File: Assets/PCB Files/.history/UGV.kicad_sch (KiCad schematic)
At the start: 68 parts, among them J10 B2B-XH-A, J11 B2B-XH-A, J12 B2B-XH-A, J13 USB3_A, J14 XT30PW-M, J15 Screw_Terminal_01x12, J16 Screw_Terminal_01x12, J17 Screw_Terminal_01x12, J18 Screw_Terminal_01x12, J19 XT30PW-M, J2 Conn_01x24_Socket, J20 XT30PW-M, J21 XT30PW-M, J22 Conn_01x01_Socket, J23 Conn_01x01_Socket, J24 XT30PW-M, J25 B2B-XH-A, J26 B2B-XH-A, J27 B2B-XH-A, J28 B2B-XH-A, J29 B2B-XH-A, J3 Conn_01x24_Socket, J31 B2B-XH-A, J4 Conn_01x02_Pin, J5 B2B-XH-A, J6 B2B-XH-A, J7 B2B-XH-A, J8 B2B-XH-A, J9 B2B-XH-A, Q1 IRLZ44N, U2 LMR33630ADDA, U3 SN74LVC8T245, U4 Teensy4.1

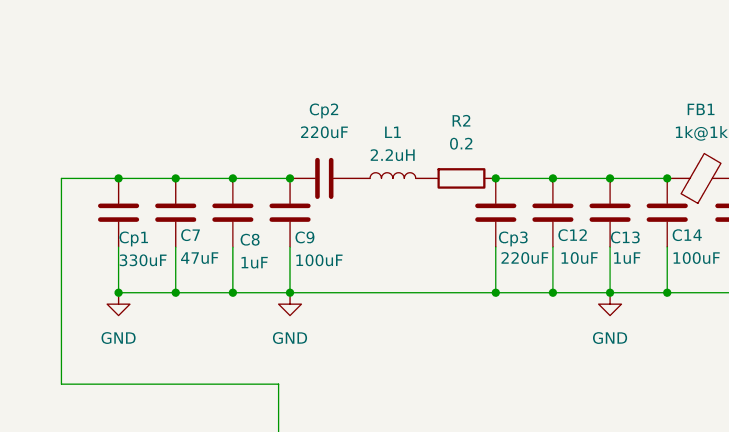
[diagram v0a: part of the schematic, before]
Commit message: Changed Capacitor in LC Filtering
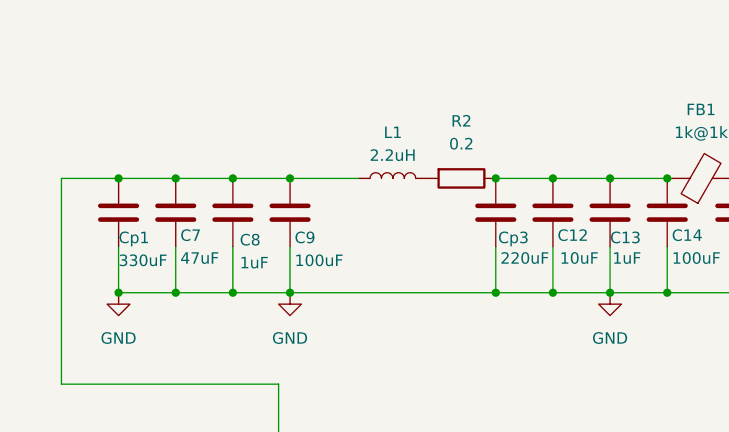
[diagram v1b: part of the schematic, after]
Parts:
- removed Cp2: 220uF, symbol Device:C
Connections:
- net at L1.1: now also C7.1, C8.1, C9.1, Cp1.1, J20.P
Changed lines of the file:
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@@
 	)
 	(junction
-		(at 43.18 27.94)
-		(diameter 0)
-		(color 0 0 0 0)
-	)
-	(junction
 		(at 91.44 120.65)
 		(diameter 0)
@@
 	)
 	(junction
+		(at 43.18 27.94)
+		(diameter 0)
+		(color 0 0 0 0)
+	)
+	(junction
 		(at 229.87 104.14)
 		(diameter 0)
@@
 	(wire
 		(pts
+			(xy 43.18 27.94) (xy 50.8 27.94)
+		)
+		(stroke
+			(width 0)
+			(type default)
+		)
+	)
+	(wire
+		(pts
 			(xy 92.71 40.64) (xy 99.06 40.64)
 		)
@@
 					(unit 1)
 				)
-			)
-		)
-	)
-	(symbol
-		(lib_id "Device:C")
-		(at 46.99 27.94 90)
-		(unit 1)
-		(body_style 1)
-		(exclude_from_sim no)
-		(in_bom yes)
-		(on_board yes)
-		(in_pos_files yes)
-		(dnp no)
-		(fields_autoplaced yes)
-		(property "Reference" "Cp2"
-			(at 46.99 20.32 90)
-			(show_name no)
-			(do_not_autoplace no)
-			(effects
-				(font
-					(size 1.27 1.27)
-				)
-			)
-		)
-		(property "Value" "220uF"
-			(at 46.99 22.86 90)
-			(show_name no)
-			(do_not_autoplace no)
-			(effects
-				(font
-					(size 1.27 1.27)
-				)
-			)
-		)
-		(property "Footprint" ""
-			(at 50.8 26.9748 0)
-			(hide yes)
-			(show_name no)
-			(do_not_autoplace no)
-			(effects
-				(font
-					(size 1.27 1.27)
-				)
-			)
-		)
-		(property "Datasheet" ""
-			(at 46.99 27.94 0)
-			(hide yes)
-			(show_name no)
-			(do_not_autoplace no)
-			(effects
-				(font
-					(size 1.27 1.27)
-				)
-			)
-		)
-		(property "Description" "Unpolarized capacitor"
-			(at 46.99 27.94 0)
-			(hide yes)
-			(show_name no)
-			(do_not_autoplace no)
-			(effects
-				(font
-					(size 1.27 1.27)
-				)
-			)
-		)
-		(pin "2"
-		)
-		(pin "1"
-		)
-		(instances
-			(project "UGV"
-				(path "/07a8edf5-8ac1-4cc3-b758-10bf557c0053"
-					(reference "Cp2")
-					(unit 1)
-				)

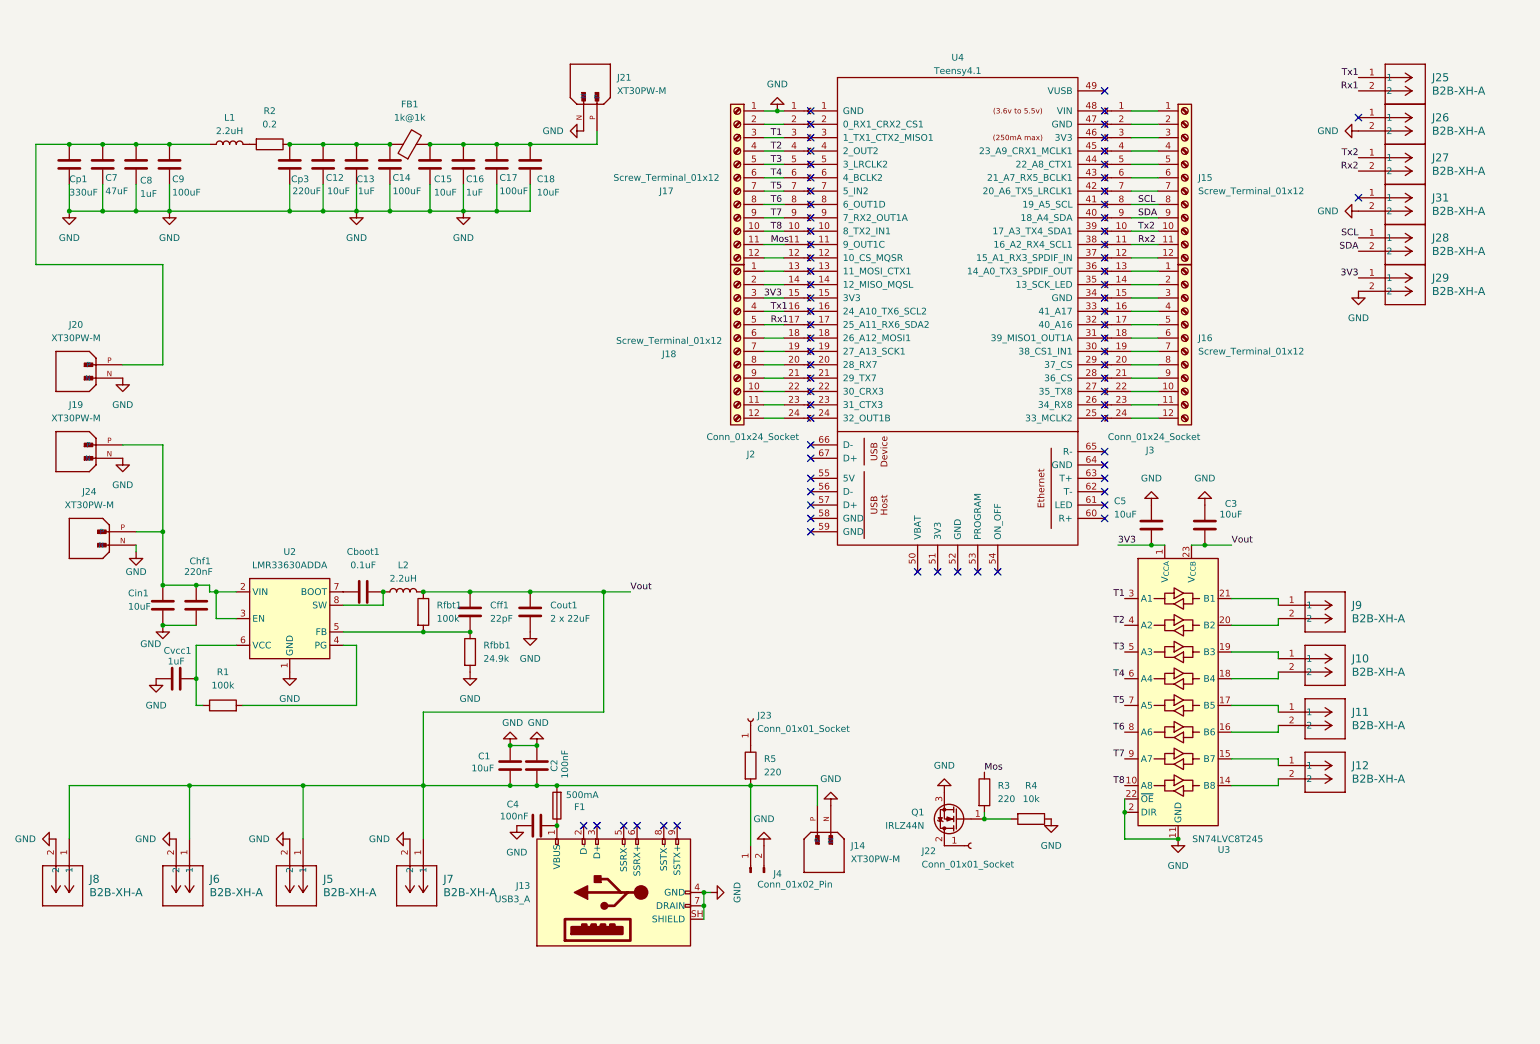
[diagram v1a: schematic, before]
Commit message: Added Custom Model and Updated PCB
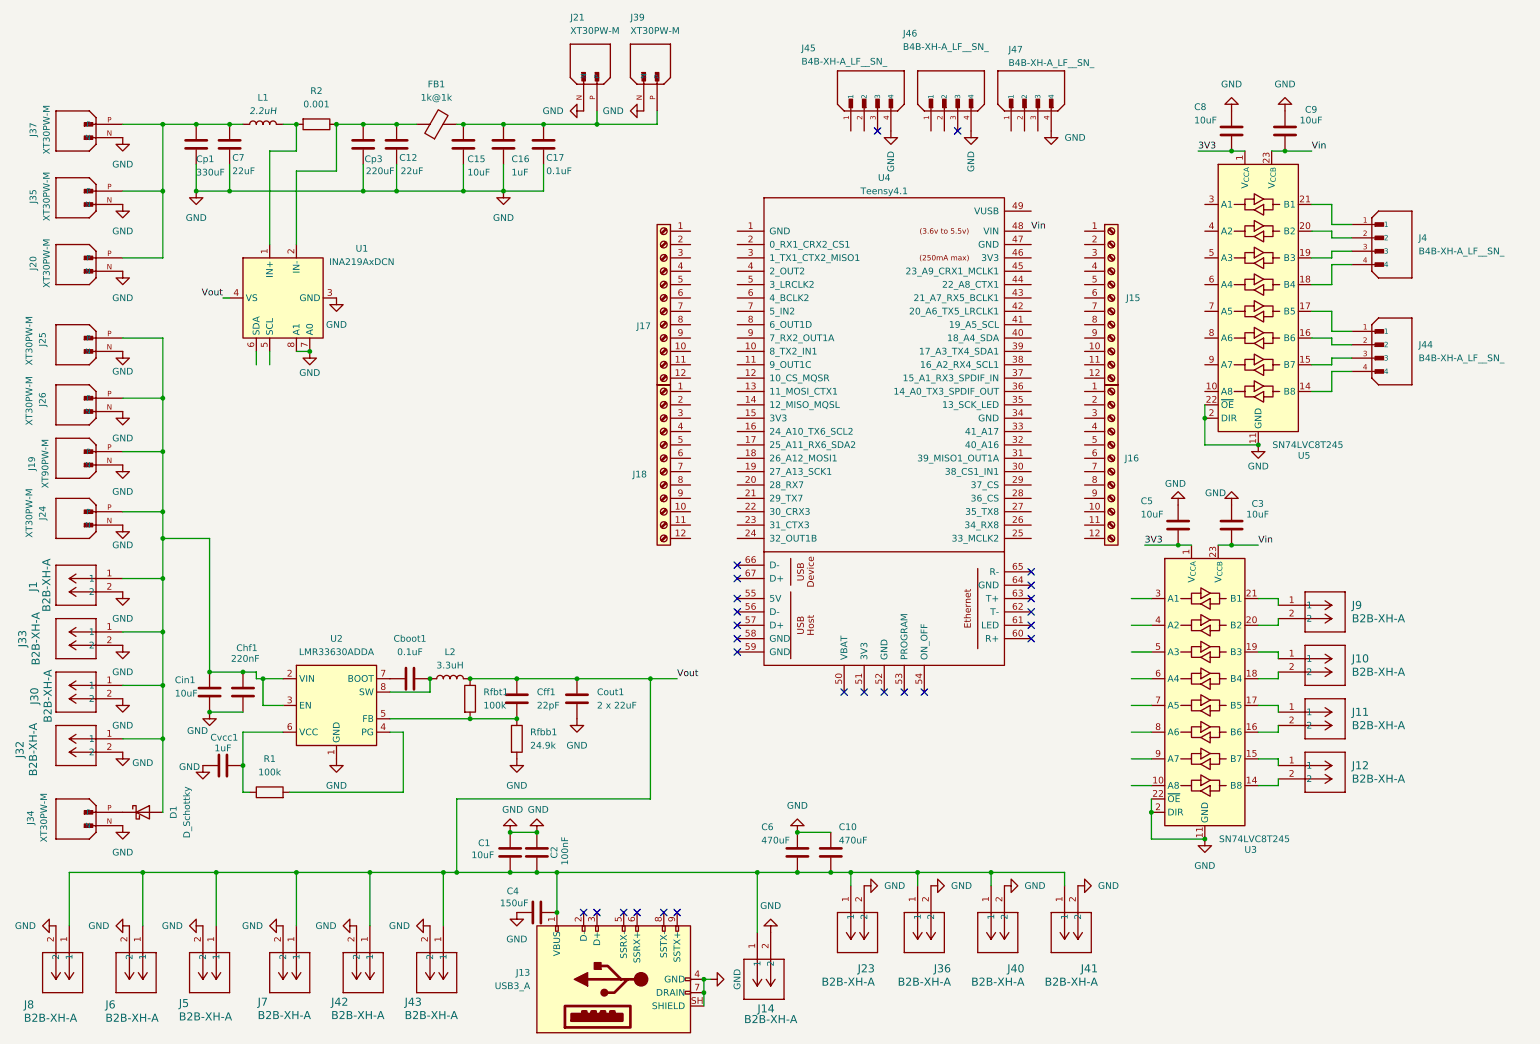
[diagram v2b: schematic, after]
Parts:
- removed C13: 1uF, symbol Device:C
- removed C14: 100uF, symbol Device:C
- removed C18: 10uF, symbol Device:C
- removed F1: 500mA, symbol Device:Fuse
- removed J14: XT30PW-M, Connector_AMASS:AMASS_XT30PW-M_1x02_P2.50mm_Horizontal, symbol XT30PW-M:XT30PW-M
- removed J2, J3: Conn_01x24_Socket, symbol Connector:Conn_01x24_Socket
- removed J22, J23: Conn_01x01_Socket, symbol Connector:Conn_01x01_Socket
- removed J25, J26, J27, J28, J29, J31: B2B-XH-A, Connector_JST:JST_XH_B2B-XH-A_1x02_P2.50mm_Vertical, symbol 2026-03-24_19-43-02:B2B-XH-A
- removed J4: Conn_01x02_Pin, symbol Connector:Conn_01x02_Pin
- removed Q1: IRLZ44N, Package_TO_SOT_THT:TO-220-3_Vertical, symbol Transistor_FET:IRLZ44N
- removed R3, R5: 220, symbol Device:R
- removed R4: 10k, symbol Device:R
- added C10, C6: 470uF, Capacitor_THT:CP_Radial_D8.0mm_P3.50mm, symbol Device:C
- added D1: D_Schottky, Diode_SMD:D_SMC_Handsoldering, symbol Device:D_Schottky
- added J1, J14, J23, J30, J32, J33, J36, J40, J41, J42, J43: B2B-XH-A, Connector_JST:JST_XH_B2B-XH-A_1x02_P2.50mm_Vertical, symbol 2026-03-24_19-43-02:B2B-XH-A
- added J25, J26, J34, J35, J37, J39: XT30PW-M, XT30PW-M (1):AMASS_XT30PW-M, symbol XT30PW-M:XT30PW-M
- added J4, J44, J45, J46, J47: B4B-XH-A_LF__SN_, B4B-XH-A_LF__SN_:JST_B4B-XH-A_LF__SN_, symbol B4B-XH-A_LF__SN_:B4B-XH-A_LF__SN_
- added U1: INA219AxDCN, Package_TO_SOT_SMD:SOT-23-8, symbol Sensor_Energy:INA219AxDCN
- added U5: SN74LVC8T245, SN74LVC8T245DWR:SOIC127P1030X265-24N, symbol Logic_LevelTranslator:SN74LVC8T245
- C1, C15, C3, C5, Cin1: footprint (none) -> Capacitor_SMD:C_1210_3225Metric
- C12: value 10uF -> 22uF; footprint (none) -> Capacitor_SMD:C_1210_3225Metric
- C16, C2, Cboot1, Cff1, Cvcc1: footprint (none) -> Capacitor_SMD:C_0603_1608Metric
- C17: value 100uF -> 0.1uF; footprint (none) -> Capacitor_SMD:C_0603_1608Metric
- C4: value 100nF -> 150uF; footprint (none) -> Capacitor_SMD:CP_Elec_8x10.5
- C7: value 47uF -> 22uF; footprint (none) -> Capacitor_SMD:C_1210_3225Metric
- C8: value 1uF -> 10uF; footprint (none) -> Capacitor_SMD:C_1210_3225Metric
- C9: value 100uF -> 10uF; footprint (none) -> Capacitor_SMD:C_1210_3225Metric
- Chf1: footprint (none) -> Capacitor_SMD:C_1206_3216Metric
- Cout1: footprint (none) -> Capacitor_SMD:C_0603_1608Metric_Pad1.08x0.95mm_HandSolder
- Cp1: footprint (none) -> Capacitor_THT:CP_Radial_D10.0mm_P5.00mm
- Cp3: footprint (none) -> Capacitor_SMD:CP_Elec_10x10
- FB1: footprint (none) -> BLM21PG220SN1D:BEADC2012X105N
- J13: footprint (none) -> EasyEDA_Lib:USB-3.0-TH_U233-091N-4BLPC17-11
- J15, J16, J17, J18: footprint (none) -> TerminalBlock_Phoenix:TerminalBlock_Phoenix_MPT-0,5-12-2.54_1x12_P2.54mm_Horizontal
- J19: value XT30PW-M -> XT90PW-M; footprint Connector_AMASS:AMASS_XT30PW-M_1x02_P2.50mm_Horizontal -> XT90PW-M:AMASS_XT90PW-M
- J20, J21, J24: footprint Connector_AMASS:AMASS_XT30PW-M_1x02_P2.50mm_Horizontal -> XT30PW-M (1):AMASS_XT30PW-M
- L1: footprint (none) -> Inductor_SMD:L_Vishay_IHLP-2525
- L2: value 2.2uH -> 3.3uH; footprint (none) -> Inductor_SMD:L_Vishay_IHLP-2525
- R1, Rfbb1, Rfbt1: footprint (none) -> Resistor_SMD:R_0402_1005Metric
- R2: value 0.2 -> 0.001; footprint (none) -> Resistor_SMD:R_0402_1005Metric
- U2: footprint Package_SO:Texas_HSOP-8-1EP_3.9x4.9mm_P1.27mm_ThermalVias -> LMR33630AQRNXTQ1:CONV_LMR33620BRNXT
- U3: footprint (none) -> SN74LVC8T245DWR:SOIC127P1030X265-24N
- U4: footprint (none) -> teensy.pretty-master:Teensy41
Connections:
- net 3V3: now also C8.2, U5.1 (V_{CCA}); no longer J18.3 (Pin_3)
- net GND: now also C8.1, C9.1, C10.1, C6.1, J1.2, J14.2, J23.2, J25.N, J26.N, J30.2, J32.2, J33.2, J34.N, J35.N, J36.2, J37.N, J39.N, J40.2, J41.2, J42.2, J43.2, J45.4, J46.4, J47.4, U1.3 (GND), U1.7 (A0), U1.8 (A1), U5.11 (GND), U5.12 (GND), U5.13 (GND), U5.2 (DIR), U5.22 (~{OE}); no longer C8.2, C9.2, J17.1 (Pin_1)
- net Vout: now also C4.2, J13.1 (VBUS), C10.2, C6.2, J14.1, J23.1, J36.1, J40.1, J41.1, J42.1, J43.1, U1.4 (VS); no longer C3.2, U3.23 (V_{CCB}), U3.24 (V_{CCB})
- net at C7.1, Cp1.1, J20.P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: now also J35.P, J37.P; no longer C8.1, C9.1
- net at L1.2, R2.2: now also U1.1 (IN+)
- net at Chf1.1, Cin1.1, J19.P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: now also D1.2 (A), J1.1, J25.P, J26.P, J30.1, J32.1, J33.1
- net at C12.1, Cp3.1, FB1.1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: now also U1.2 (IN-)
- net at C15.1, C16.1, C17.1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: now also J39.P
- net Vin: now reaches U4.48 (VIN)
- net Vin: now also C3.2, C9.2, U3.23 (V_{CCB}), U3.24 (V_{CCB}), U5.23 (V_{CCB}), U5.24 (V_{CCB})
- net Mos: no longer names the net of J17.11 (Pin_11)
- net Rx1: no longer names the net of J18.5 (Pin_5)
- net Rx2: no longer names the net of J15.11 (Pin_11)
- net SCL: no longer names the net of J15.8 (Pin_8)
- net SDA: no longer names the net of J15.9 (Pin_9)
- net T1: no longer names the net of U3.3 (A1)
- net T1: no longer J17.3 (Pin_3)
- net T2: no longer names the net of U3.4 (A2)
- net T2: no longer J17.4 (Pin_4)
- net T3: no longer names the net of U3.5 (A3)
- net T3: no longer J17.5 (Pin_5)
- net T4: no longer names the net of U3.6 (A4)
- net T4: no longer J17.6 (Pin_6)
- net T5: no longer names the net of U3.7 (A5)
- net T5: no longer J17.7 (Pin_7)
- net T6: no longer names the net of U3.8 (A6)
- net T6: no longer J17.8 (Pin_8)
- net T7: no longer names the net of U3.9 (A7)
- net T7: no longer J17.9 (Pin_9)
- net T8: no longer names the net of U3.10 (A8)
- net T8: no longer J17.10 (Pin_10)
- net Tx1: no longer names the net of J18.4 (Pin_4)
- net Tx2: no longer names the net of J15.10 (Pin_10)
- new net: J44.4, U5.14 (B8)
- new net: J44.3, U5.15 (B7)
- new net: J44.2, U5.16 (B6)
- new net: J44.1, U5.17 (B5)
- new net: J4.4, U5.18 (B4)
- new net: J4.3, U5.19 (B3)
- new net: J4.2, U5.20 (B2)
- new net: J4.1, U5.21 (B1)
- new net: D1.1 (K), J34.P
- no-connect marks 75 -> 26
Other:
- moved on the sheet: C1, C12, C15, C16, C17, C2, C3, C4, C5, C7, Cboot1, Cff1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
